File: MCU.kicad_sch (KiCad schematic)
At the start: 48 parts, among them SW1 RotaryEncoder_Switch, U4 MIC5219-3.3YM5

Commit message: Layout Routing is 50% complete
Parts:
- removed MT1: PEC11R-4215F-S0024, Rotary_Encoder:RotaryEncoder_Alps_EC11E_Vertical_H20mm, symbol RotaryEncoder:PEC11R-4215F-S0024
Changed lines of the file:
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@@
-    )
-  )
-  (symbol (lib_id "RotaryEncoder:PEC11R-4215F-S0024") (at 196.85 73.66 0) (unit 1)
-    (in_bom yes) (on_board yes) (dnp no)
-    (property "Reference" "MT1" (at 196.85 63.5 0)
-      (effects (font (size 1.27 1.27)))
-    )
-    (property "Value" "PEC11R-4215F-S0024" (at 196.85 83.82 0)
-      (effects (font (size 1.27 1.27)))
-    )
-    (property "Footprint" "Rotary_Encoder:RotaryEncoder_Alps_EC11E_Vertical_H20mm" (at 196.85 73.66 0)
-      (effects (font (size 1.27 1.27)) (justify bottom) hide)
-    )
-    (property "Datasheet" "" (at 196.85 73.66 0)
-      (effects (font (size 1.27 1.27)) hide)
-    )
-    (property "MF" "Bourns" (at 196.85 73.66 0)
-      (effects (font (size 1.27 1.27)) (justify bottom) hide)
-    )
-    (property "MAXIMUM_PACKAGE_HEIGHT" "21.5 mm" (at 196.85 73.66 0)
-      (effects (font (size 1.27 1.27)) (justify bottom) hide)
-    )
-    (property "Package" "None" (at 196.85 73.66 0)
-      (effects (font (size 1.27 1.27)) (justify bottom) hide)
-    )
-    (property "Price" "None" (at 196.85 73.66 0)
-      (effects (font (size 1.27 1.27)) (justify bottom) hide)
-    )
-    (property "Check_prices" "https://www.snapeda.com/parts/PEC11R-4215F-S0024/Bourns/view-part/?ref=eda" (at 196.85 73.66 0)
-      (effects (font (size 1.27 1.27)) (justify bottom) hide)
-    )
-    (property "STANDARD" "Manufacturer Recommendations" (at 196.85 73.66 0)
-      (effects (font (size 1.27 1.27)) (justify bottom) hide)
-    )
-    (property "PARTREV" "Rev. 09/19" (at 196.85 73.66 0)
-      (effects (font (size 1.27 1.27)) (justify bottom) hide)
-    )
-    (property "SnapEDA_Link" "https://www.snapeda.com/parts/PEC11R-4215F-S0024/Bourns/view-part/?ref=snap" (at 196.85 73.66 0)
-      (effects (font (size 1.27 1.27)) (justify bottom) hide)
-    )
-    (property "MP" "PEC11R-4215F-S0024" (at 196.85 73.66 0)
-      (effects (font (size 1.27 1.27)) (justify bottom) hide)
-    )
-    (property "Purchase-URL" "https://www.snapeda.com/api/url_track_click_mouser/?unipart_id=428605&manufacturer=Bourns&part_name=PEC11R-4215F-S0024&search_term=None" (at 196.85 73.66 0)
-      (effects (font (size 1.27 1.27)) (justify bottom) hide)
-    )
-    (property "Description" "\nEncoder,Rotary,24 Detents,15 mm, Shaft,Switch | Bourns PEC11R-4215F-S0024\n" (at 196.85 73.66 0)
-      (effects (font (size 1.27 1.27)) (justify bottom) hide)
-    )
-    (property "Availability" "In Stock" (at 196.85 73.66 0)
-      (effects (font (size 1.27 1.27)) (justify bottom) hide)
-    )
-    (property "MANUFACTURER" "J.W.Miller/Bourns" (at 196.85 73.66 0)
-      (effects (font (size 1.27 1.27)) (justify bottom) hide)
-    )
-    (pin "1")
-    (pin "2")
-    (pin "A")
-    (pin "B")
-    (pin "COM")
-    (pin "S1")
-    (pin "S2")
-    (instances
-      (project "Light-CC"
-        (path "/a3254443-8240-44f0-af35-274db02f779b/04c702c6-04db-4682-92c6-1d956531dc1e"
-          (reference "MT1") (unit 1)
-        )
-      )
     )
   )

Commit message: Layout & routing is almost done Logo need to added
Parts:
- SW1: footprint Rotary_Encoder:RotaryEncoder_Alps_EC11E_Vertical_H20mm -> Rotary_Encoder:RotaryEncoder_Alps_EC12E-Switch_Vertical_H20mm
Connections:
- net HAP_PWM: now also U?.39 (GPIO27_ADC1); no longer U?.29 (GPIO18)
- net LED1: now also U?.29 (GPIO18); no longer U?.8 (GPIO6)
- net LED2: now also U?.30 (GPIO19); no longer U?.7 (GPIO5)
- net LED3: now also U?.31 (GPIO20); no longer U?.6 (GPIO4)
- net LED_PWM: now also U?.38 (GPIO26_ADC0); no longer U?.30 (GPIO19)
- net RE1: now also U?.36 (GPIO24); no longer U?.41 (GPIO29_ADC3)
- net RE2: now also U?.35 (GPIO23); no longer U?.40 (GPIO28_ADC2)
- net RE_SW: now also U?.37 (GPIO25); no longer U?.39 (GPIO27_ADC1)
- no-connect marks 25 -> 22
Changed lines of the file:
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@@
   (junction (at 234.95 48.26) (diameter 0) (color 0 0 0 0)
   )
+  (no_connect (at 152.4 127))
   (no_connect (at 152.4 106.68))
-  (no_connect (at 152.4 101.6))
   (no_connect (at 152.4 73.66))
   (no_connect (at 152.4 78.74))
@@
   (no_connect (at 152.4 53.34))
   (no_connect (at 154.94 173.99))
+  (no_connect (at 152.4 124.46))
   (no_connect (at 152.4 86.36))
   (no_connect (at 152.4 55.88))
-  (no_connect (at 152.4 104.14))
-  (no_connect (at 152.4 111.76))
-  (no_connect (at 152.4 119.38))
-  (no_connect (at 152.4 109.22))
-  (no_connect (at 152.4 114.3))
   (no_connect (at 152.4 76.2))
   (no_connect (at 152.4 71.12))
+  (no_connect (at 152.4 104.14))
   (no_connect (at 152.4 81.28))
   (no_connect (at 152.4 83.82))
@@
     (stroke (width 0) (type default))
   )
-  (wire (pts (xy 161.29 121.92) (xy 152.4 121.92))
+  (wire (pts (xy 161.29 99.06) (xy 152.4 99.06))
     (stroke (width 0) (type default))
   )
@@
     (stroke (width 0) (type default))
   )
-  (wire (pts (xy 152.4 99.06) (xy 156.21 99.06))
-    (stroke (width 0) (type default))
-  )
   (wire (pts (xy 50.8 109.22) (xy 55.88 109.22))
     (stroke (width 0) (type default))
@@
     (stroke (width 0) (type default))
   )
+  (wire (pts (xy 161.29 101.6) (xy 152.4 101.6))
+    (stroke (width 0) (type default))
+  )
   (wire (pts (xy 139.7 173.99) (xy 137.16 173.99))
     (stroke (width 0) (type default))
   )
-  (wire (pts (xy 161.29 60.96) (xy 152.4 60.96))
+  (wire (pts (xy 161.29 109.22) (xy 152.4 109.22))
     (stroke (width 0) (type default))
   )
@@
     (stroke (width 0) (type default))
   )
+  (wire (pts (xy 152.4 119.38) (xy 157.48 119.38))
+    (stroke (width 0) (type default))
+  )
   (wire (pts (xy 259.08 49.53) (xy 259.08 44.45))
     (stroke (width 0) (type default))
@@
     (stroke (width 0) (type default))
   )
+  (wire (pts (xy 161.29 96.52) (xy 152.4 96.52))
+    (stroke (width 0) (type default))
+  )
   (wire (pts (xy 251.46 48.26) (xy 251.46 50.8))
     (stroke (width 0) (type default))
   )
-  (wire (pts (xy 152.4 96.52) (xy 156.21 96.52))
-    (stroke (width 0) (type default))
-  )
   (wire (pts (xy 52.07 166.37) (xy 52.07 167.64))
     (stroke (width 0) (type default))
@@
     (stroke (width 0) (type default))
   )
-  (wire (pts (xy 161.29 63.5) (xy 152.4 63.5))
-    (stroke (width 0) (type default))
-  )
   (wire (pts (xy 259.08 44.45) (xy 251.46 44.45))
     (stroke (width 0) (type default))
   )
-  (wire (pts (xy 161.29 127) (xy 152.4 127))
+  (wire (pts (xy 161.29 114.3) (xy 152.4 114.3))
     (stroke (width 0) (type default))
   )
@@
     (stroke (width 0) (type default))
   )
+  (wire (pts (xy 161.29 111.76) (xy 152.4 111.76))
+    (stroke (width 0) (type default))
+  )
   (wire (pts (xy 151.13 34.29) (xy 151.13 35.56))
     (stroke (width 0) (type default))
@@
     (stroke (width 0) (type default))
   )
+  (wire (pts (xy 152.4 121.92) (xy 157.48 121.92))
+    (stroke (width 0) (type default))
+  )
   (wire (pts (xy 132.08 40.64) (xy 132.08 43.18))
     (stroke (width 0) (type default))
   )
-  (wire (pts (xy 161.29 66.04) (xy 152.4 66.04))
-    (stroke (width 0) (type default))
-  )
   (wire (pts (xy 251.46 60.96) (xy 259.08 60.96))
-    (stroke (width 0) (type default))
-  )
-  (wire (pts (xy 161.29 124.46) (xy 152.4 124.46))
     (stroke (width 0) (type default))
   )
@@
     (effects (font (size 1.27 1.27)) (justify left bottom))
   )
+  (label "LED3" (at 161.29 101.6 180) (fields_autoplaced)
+    (effects (font (size 1.27 1.27)) (justify right bottom))
+  )
   (label "RUN" (at 30.48 31.75 0) (fields_autoplaced)
     (effects (font (size 1.27 1.27)) (justify left bottom))
@@
     (effects (font (size 1.27 1.27)) (justify left bottom))
   )
+  (label "RE_SW" (at 161.29 114.3 180) (fields_autoplaced)
+    (effects (font (size 1.27 1.27)) (justify right bottom))
+  )
   (label "SD1" (at 55.88 111.76 180) (fields_autoplaced)
     (effects (font (size 1.27 1.27)) (justify right bottom))
@@
     (effects (font (size 1.27 1.27)) (justify left bottom))
   )
-  (label "RE1" (at 161.29 127 180) (fields_autoplaced)
-    (effects (font (size 1.27 1.27)) (justify right bottom))
-  )
   (label "B1" (at 265.43 157.48 0) (fields_autoplaced)
     (effects (font (size 1.27 1.27)) (justify left bottom))
@@
     (effects (font (size 1.27 1.27)) (justify right bottom))
   )
+  (label "LED2" (at 161.29 99.06 180) (fields_autoplaced)
+    (effects (font (size 1.27 1.27)) (justify right bottom))
+  )
   (label "D-" (at 57.15 166.37 180) (fields_autoplaced)
     (effects (font (size 1.27 1.27)) (justify right bottom))
@@
     (effects (font (size 1.27 1.27)) (justify left bottom))
   )
-  (label "LED3" (at 161.29 60.96 180) (fields_autoplaced)
+  (label "LED1" (at 161.29 96.52 180) (fields_autoplaced)
     (effects (font (size 1.27 1.27)) (justify right bottom))
   )
@@
     (effects (font (size 1.27 1.27)) (justify right bottom))
   )
-  (label "LED1" (at 161.29 66.04 180) (fields_autoplaced)
-    (effects (font (size 1.27 1.27)) (justify right bottom))
-  )
   (label "SD3" (at 55.88 119.38 180) (fields_autoplaced)
     (effects (font (size 1.27 1.27)) (justify right bottom))
@@
     (effects (font (size 1.27 1.27)) (justify left bottom))
   )
+  (label "RE2" (at 161.29 109.22 180) (fields_autoplaced)
+    (effects (font (size 1.27 1.27)) (justify right bottom))
+  )
   (label "LED3" (at 245.11 129.54 0) (fields_autoplaced)
     (effects (font (size 1.27 1.27)) (justify left bottom))
@@
     (effects (font (size 1.27 1.27)) (justify left bottom))
   )
-  (label "RE_SW" (at 161.29 121.92 180) (fields_autoplaced)
-    (effects (font (size 1.27 1.27)) (justify right bottom))
-  )
-  (label "LED2" (at 161.29 63.5 180) (fields_autoplaced)
+  (label "RE1" (at 161.29 111.76 180) (fields_autoplaced)
     (effects (font (size 1.27 1.27)) (justify right bottom))
   )
@@
     (effects (font (size 1.27 1.27)) (justify left bottom))
   )
-  (label "RE2" (at 161.29 124.46 180) (fields_autoplaced)
-    (effects (font (size 1.27 1.27)) (justify right bottom))
-  )
   (label "RE1" (at 234.95 50.8 0) (fields_autoplaced)
     (effects (font (size 1.27 1.27)) (justify left bottom))
   )
-  (hierarchical_label "HAP_PWM" (shape output) (at 156.21 96.52 0) (fields_autoplaced)
+  (hierarchical_label "HAP_PWM" (shape output) (at 157.48 121.92 0) (fields_autoplaced)
     (effects (font (size 1.27 1.27)) (justify left))
   )
-  (hierarchical_label "LED_PWM" (shape output) (at 156.21 99.06 0) (fields_autoplaced)
+  (hierarchical_label "LED_PWM" (shape output) (at 157.48 119.38 0) (fields_autoplaced)
     (effects (font (size 1.27 1.27)) (justify left))
   )
@@
       (effects (font (size 1.27 1.27)))
     )
-    (property "Footprint" "Rotary_Encoder:RotaryEncoder_Alps_EC11E_Vertical_H20mm" (at 217.17 49.784 0)
-      (effects (font (size 1.27 1.27)) hide)
-    )
+    (property "Footprint" "Rotary_Encoder:RotaryEncoder_Alps_EC12E-Switch_Vertical_H20mm" (at 217.17 49.784 0)
+      (effects (font (size 1.27 1.27)) hide)
+    )

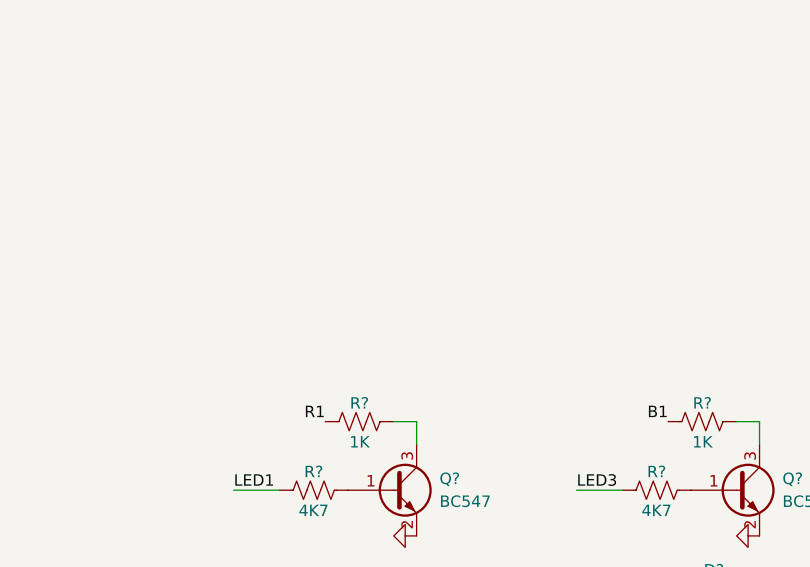
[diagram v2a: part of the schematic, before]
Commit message: Pwr led added
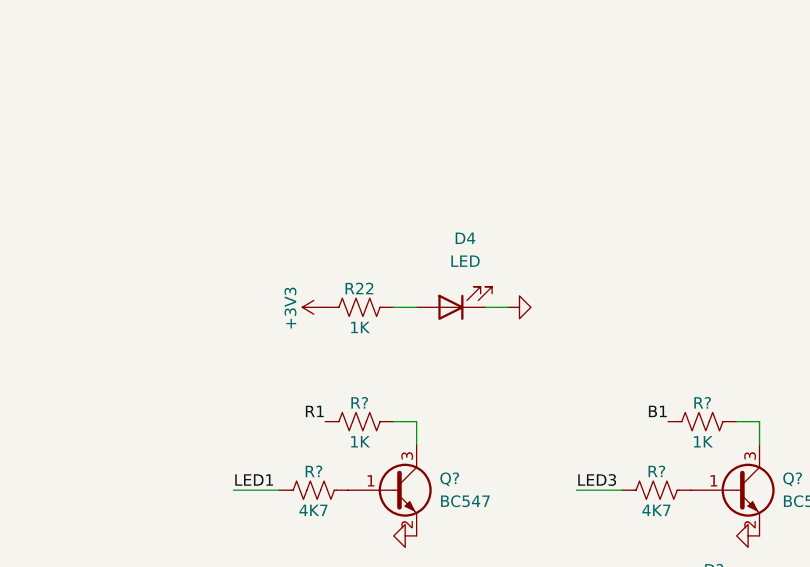
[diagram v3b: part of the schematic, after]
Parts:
- added D4: LED, symbol Device:LED
- added R22: 1K, Resistor_SMD:R_0603_1608Metric, symbol Device:R_US
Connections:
- net +3V3: now also R22.1
- net GND: now also D4.1 (K)
- new net: D4.2 (A), R22.2
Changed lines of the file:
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@@
+    (stroke (width 0) (type default))
+  )
+  (wire (pts (xy 224.79 109.22) (xy 227.33 109.22))
     (stroke (width 0) (type default))
   )
@@
   )
   (wire (pts (xy 158.75 171.45) (xy 161.29 171.45))
+    (stroke (width 0) (type default))
+  )
+  (wire (pts (xy 234.95 109.22) (xy 237.49 109.22))
     (stroke (width 0) (type default))
   )
@@
         (path "/a3254443-8240-44f0-af35-274db02f779b/04c702c6-04db-4682-92c6-1d956531dc1e"
           (reference "R21") (unit 1)
+        )
+      )
+    )
+  )
+  (symbol (lib_id "power:+3V3") (at 217.17 109.22 90) (unit 1)
+    (in_bom yes) (on_board yes) (dnp no)
+    (property "Reference" "#PWR050" (at 220.98 109.22 0)
+      (effects (font (size 1.27 1.27)) hide)
+    )
+    (property "Value" "+3V3" (at 213.36 111.76 0)
+      (effects (font (size 1.27 1.27)) (justify left))
+    )
+    (property "Footprint" "" (at 217.17 109.22 0)
+      (effects (font (size 1.27 1.27)) hide)
+    )
+    (property "Datasheet" "" (at 217.17 109.22 0)
+      (effects (font (size 1.27 1.27)) hide)
+    )
+    (pin "1")
+    (instances
+      (project "Light-CC"
+        (path "/a3254443-8240-44f0-af35-274db02f779b/04c702c6-04db-4682-92c6-1d956531dc1e"
+          (reference "#PWR050") (unit 1)
         )
       )
@@
         (path "/a3254443-8240-44f0-af35-274db02f779b/04c702c6-04db-4682-92c6-1d956531dc1e"
           (reference "U4") (unit 1)
+        )
+      )
+    )
+  )
+  (symbol (lib_id "power:GND") (at 237.49 109.22 90) (unit 1)
+    (in_bom yes) (on_board yes) (dnp no) (fields_autoplaced)
+    (property "Reference" "#PWR049" (at 243.84 109.22 0)
+      (effects (font (size 1.27 1.27)) hide)
+    )
+    (property "Value" "GND" (at 236.728 109.2201 90)
+      (effects (font (size 1.27 1.27)) (justify left) hide)
+    )
+    (property "Footprint" "" (at 237.49 109.22 0)
+      (effects (font (size 1.27 1.27)) hide)
+    )
+    (property "Datasheet" "" (at 237.49 109.22 0)
+      (effects (font (size 1.27 1.27)) hide)
+    )
+    (pin "1")
+    (instances
+      (project "Light-CC"
+        (path "/a3254443-8240-44f0-af35-274db02f779b/04c702c6-04db-4682-92c6-1d956531dc1e"
+          (reference "#PWR049") (unit 1)
         )
       )
@@
     )
   )
+  (symbol (lib_id "Device:LED") (at 231.14 109.22 180) (unit 1)
+    (in_bom yes) (on_board yes) (dnp no) (fields_autoplaced)
+    (property "Reference" "D4" (at 232.7275 101.6 0)
+      (effects (font (size 1.27 1.27)))
+    )
+    (property "Value" "LED" (at 232.7275 104.14 0)
+      (effects (font (size 1.27 1.27)))
+    )
+    (property "Footprint" "" (at 231.14 109.22 0)
+      (effects (font (size 1.27 1.27)) hide)
+    )
+    (property "Datasheet" "~" (at 231.14 109.22 0)
+      (effects (font (size 1.27 1.27)) hide)
+    )
+    (pin "1")
+    (pin "2")
+    (instances
+      (project "Light-CC"
+        (path "/a3254443-8240-44f0-af35-274db02f779b/04c702c6-04db-4682-92c6-1d956531dc1e"
+          (reference "D4") (unit 1)
+        )
+      )
+    )
+  )
   (symbol (lib_id "Device:R_US") (at 220.98 142.24 90) (unit 1)
     (in_bom yes) (on_board yes) (dnp no)
@@
         )
       )
+    )
+  )
+  (symbol (lib_id "Device:R_US") (at 220.98 109.22 90) (unit 1)
+    (in_bom yes) (on_board yes) (dnp no)
+    (property "Reference" "R22" (at 220.98 107.188 90)
+      (effects (font (size 1.27 1.27)))
+    )
+    (property "Value" "1K" (at 220.98 111.506 90)
+      (effects (font (size 1.27 1.27)))
+    )
+    (property "Footprint" "Resistor_SMD:R_0603_1608Metric" (at 221.234 108.204 90)
+      (effects (font (size 1.27 1.27)) hide)
+    )
+    (property "Datasheet" "~" (at 220.98 109.22 0)
+      (effects (font (size 1.27 1.27)) hide)
+    )
+    (pin "1")
+    (pin "2")
+    (instances
+      (project "Light-CC"
+        (path "/a3254443-8240-44f0-af35-274db02f779b/04c702c6-04db-4682-92c6-1d956531dc1e"
+          (reference "R22") (unit 1)
+        )
+      )
